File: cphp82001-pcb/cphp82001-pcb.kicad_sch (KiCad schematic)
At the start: 28 parts, among them J1 USB, J2 PAD+, J3 PAD-, Q1 2N7002, Q2 AO3413, U1 BQ21040, U2 TLV75801, U3 MAX40203AUK, U4 APX810-44SA, U5 APX809S-31SA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

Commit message: rev3.5
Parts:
- removed C2: 1n, Capacitor_SMD:C_0805_2012Metric, symbol Device:C
- added C4: 1u, Capacitor_SMD:C_0805_2012Metric, symbol Device:C
- added JP1: NOREG, Resistor_SMD:R_0603_1608Metric, symbol Jumper:SolderJumper_2_Open
- added JP2: NOLIM, Resistor_SMD:R_0603_1608Metric, symbol Jumper:SolderJumper_2_Open
- added R3: 10k, Resistor_SMD:R_0805_2012Metric, symbol Device:R
- added U7: NCP380HSN05, george:SOT-23-5_TI_DBV5, symbol kicad_george:TPS2051B
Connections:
- net EN: now also U3.3 (EN)
- net GND: now also C4.2, R3.1, U7.2 (GND)
- net VOUT: now also C4.1, JP1.2 (B), JP2.1 (A), U7.4 (EN), U7.5 (IN); no longer C7.1, D2.1 (K), J2.1 (Pin_1), U4.3 (VCC)
- net VREG: now also JP1.1 (A)
- new net: R3.2, U7.3 (~{OC})
- new net VOUTF: C7.1, D2.1 (K), J2.1 (Pin_1), JP2.2 (B), U4.3 (VCC), U7.1 (OUT)
- no-connect marks 5 -> 4
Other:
- note added: "3.0~4.2V"
- moved on the sheet: BT1, C3, C5, C7, D2, D3, J2, J3, Q2, R13, R2, R4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

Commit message: Rev 4.0
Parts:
- BT1: value LiPo -> Batt; footprint Connector_JST:JST_SH_BM03B-SRSS-TB_1x03-1MP_P1.00mm_Vertical -> george:JST_SH_BM03B-SRSS-TB_1x03-1MP_P1.00mm_Vertical_13PADS
- D1: value PMEG40T10ERX -> PMEG40T10ERX
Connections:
- net B+: now also JP1.1 (A)
- net VOUT: no longer JP1.2 (B)
- net VREG: now also JP1.2 (B); no longer JP1.1 (A)

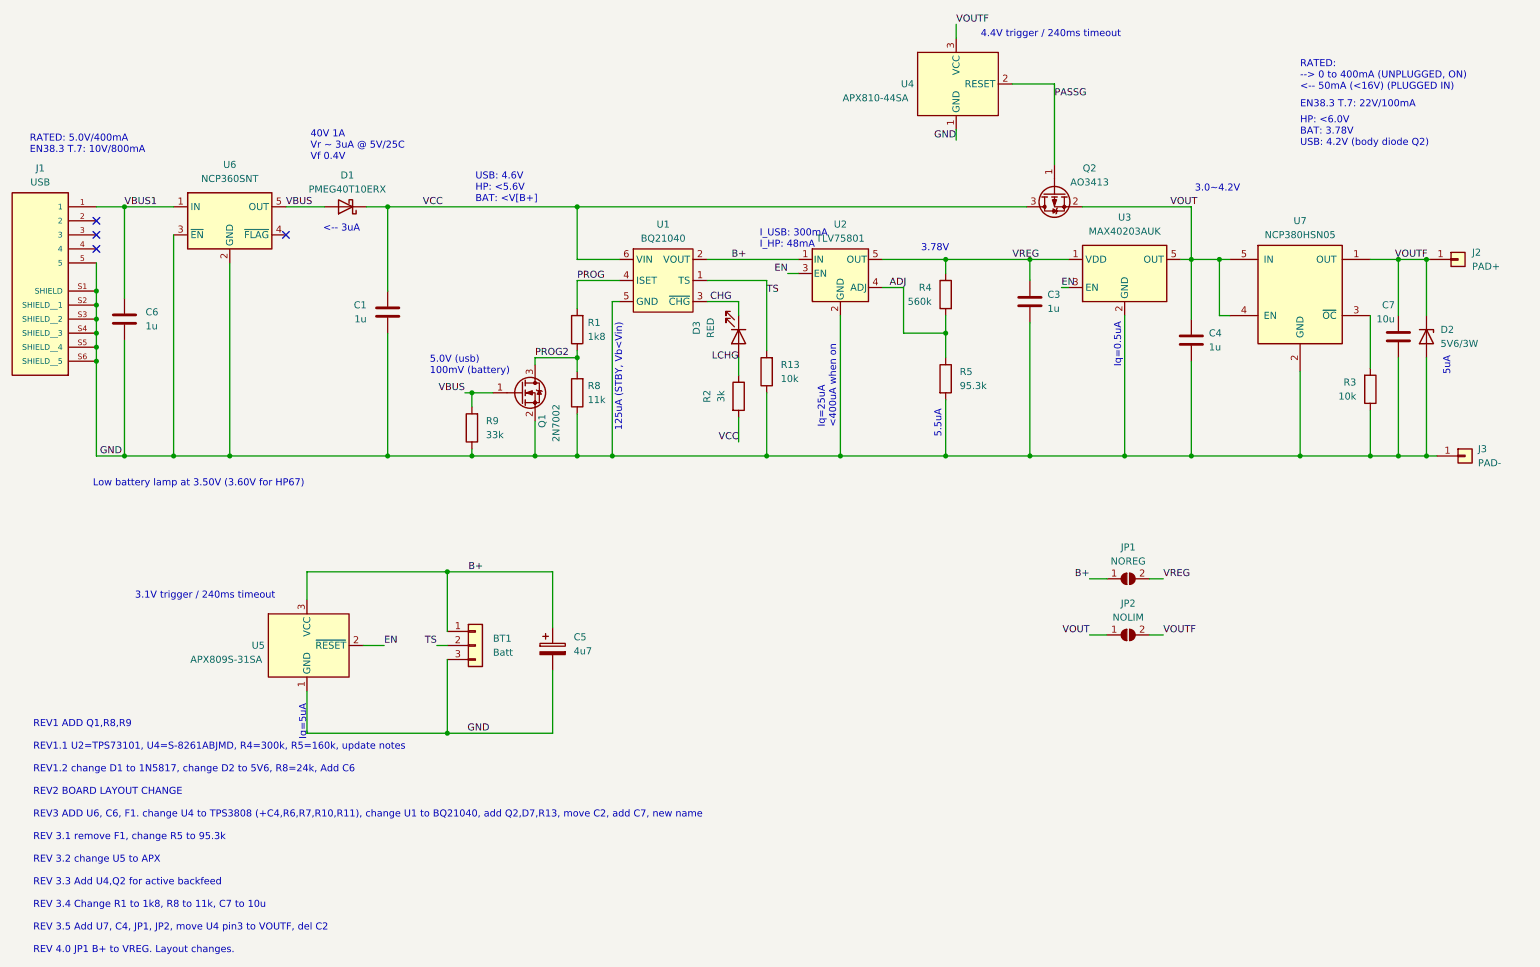
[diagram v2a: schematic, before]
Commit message: Update schematic notes
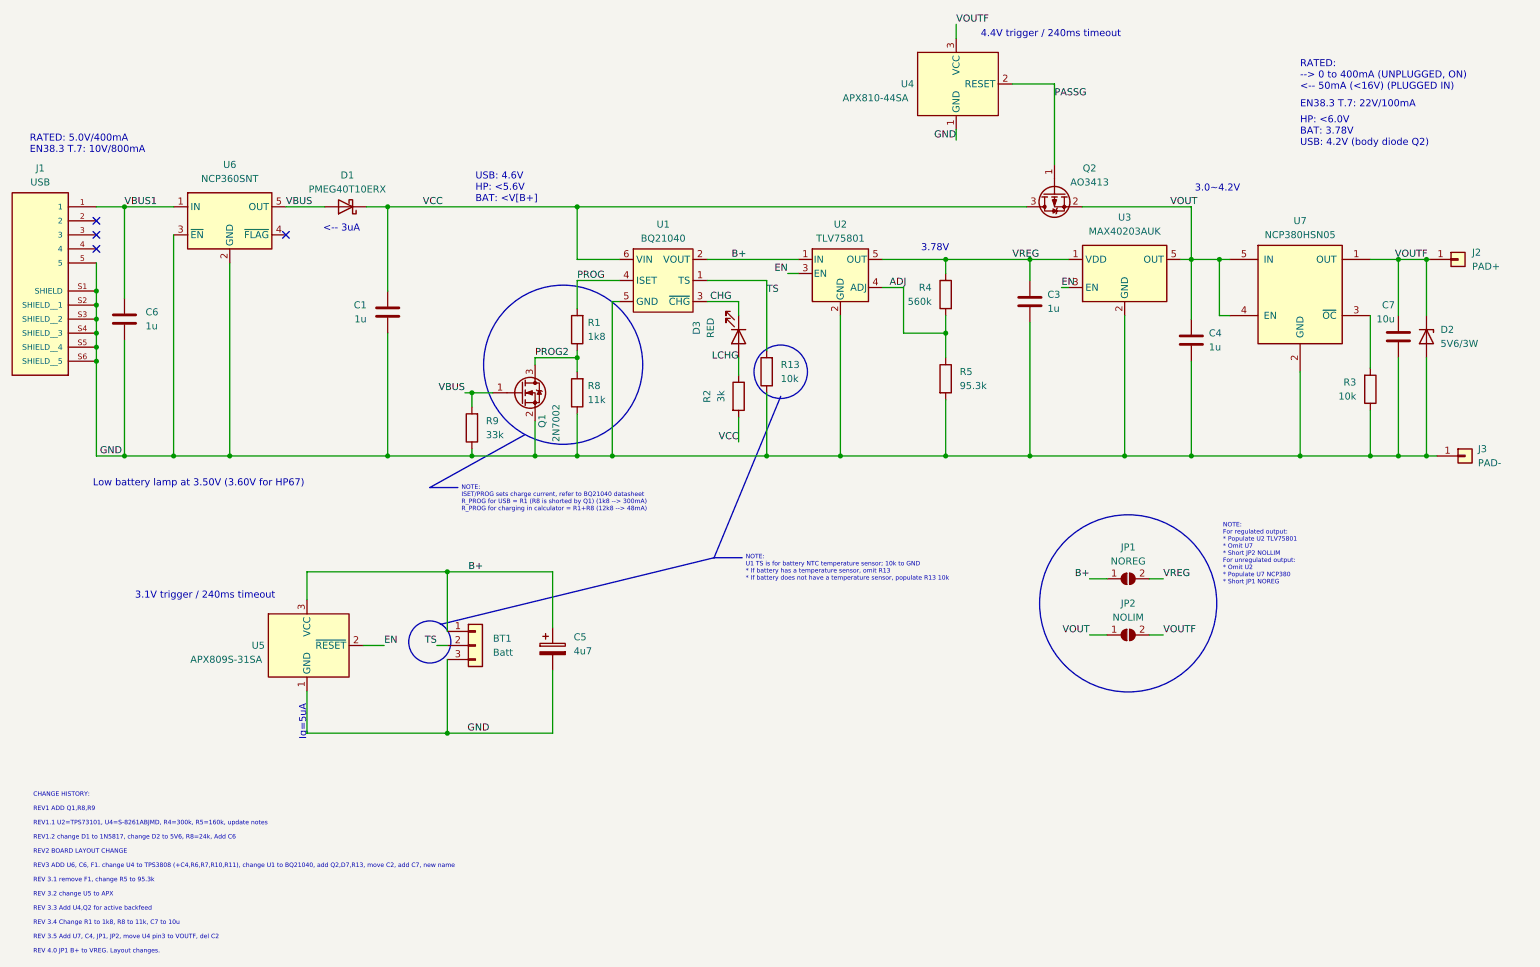
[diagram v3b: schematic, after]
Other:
- note added: "CHANGE HISTORY: REV1 ADD Q1,R8,R9 REV1.1 U2=TPS73101, U4=S-8261ABJMD, R4=300k, R5=160k, update notes REV1.2 change D1 to 1N5817, change D2 to 5V6, R8=24k, Add C6 REV2 BOARD LAYOUT CHANGE REV3 ADD U6, C6, F1. change U4 to TPS3808 (+C4,R6,R7,R10,R11), change U1 to BQ21040, add Q2,D7,R13, move C2, add C7, new name REV 3.1 remove F1, change R5 to 95.3k REV 3.2 change U5 to APX REV 3.3 Add U4,Q2 for a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"
- note added: "NOTE: For regulated output: * Populate U2 TLV75801 * Omit U7 * Short JP2 NOLLIM For unregulated output: * Omit U2 * Populate U7 NCP380 * Short JP1 NOREG"
- note added: "NOTE: ISET/PROG sets charge current, refer to BQ21040 datasheet R_PROG for USB = R1 (R8 is shorted by Q1) (1k8 --> 300mA) R_PROG for charging in calculator = R1+R8 (12k8 --> 48mA)"
- note added: "NOTE: U1 TS is for battery NTC temperature sensor; 10k to GND * If battery has a temperature sensor, omit R13 * If battery does not have a temperature sensor, populate R13 10k"
- note removed: "125uA (STBY, Vb<Vin)"
- note removed: "40V 1A Vr ~ 3uA @ 5V/25C Vf 0.4V"
- note removed: "5.0V (usb) 100mV (battery)"
- note removed: "5.5uA"
- note removed: "5uA"
- note removed: "I_USB: 300mA I_HP: 48mA"
- note removed: "Iq=0.5uA"
- note removed: "Iq=25uA <400uA when on"
- note removed: "REV1 ADD Q1,R8,R9 REV1.1 U2=TPS73101, U4=S-8261ABJMD, R4=300k, R5=160k, update notes REV1.2 change D1 to 1N5817, change D2 to 5V6, R8=24k, Add C6 REV2 BOARD LAYOUT CHANGE REV3 ADD U6, C6, F1. change U4 to TPS3808 (+C4,R6,R7,R10,R11), change U1 to BQ21040, add Q2,D7,R13, move C2, add C7, new name REV 3.1 remove F1, change R5 to 95.3k REV 3.2 change U5 to APX REV 3.3 Add U4,Q2 for active backfeed R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"
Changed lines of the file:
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@@
+		)
+	)
+	(polyline
+		(pts
+			(xy 89.535 109.855) (xy 106.68 100.33)
+		)
+		(stroke
+			(width 0)
+			(type default)
 		)
 	)
@@
 		)
 	)
+	(polyline
+		(pts
+			(xy 140.97 122.555) (xy 153.035 93.345)
+		)
+		(stroke
+			(width 0)
+			(type default)
+		)
+	)
 	(wire
 		(pts
@@
 		)
 	)
+	(polyline
+		(pts
+			(xy 91.44 134.62) (xy 140.97 122.555)
+		)
+		(stroke
+			(width 0)
+			(type default)
+		)
+	)
 	(wire
 		(pts
@@
 		)
 	)
+	(polyline
+		(pts
+			(xy 146.05 122.555) (xy 140.97 122.555)
+		)
+		(stroke
+			(width 0)
+			(type default)
+		)
+	)
 	(wire
 		(pts
@@
 		)
 	)
+	(polyline
+		(pts
+			(xy 94.615 109.855) (xy 89.535 109.855)
+		)
+		(stroke
+			(width 0)
+			(type default)
+		)
+	)
 	(wire
 		(pts
@@
 			(width 0)
 			(type default)
+		)
+	)
+	(circle
+		(center 215.9 130.81)
+		(radius 16.0267)
+		(stroke
+			(width 0)
+			(type default)
+		)
+		(fill
+			(type none)
+		)
+	)
+	(circle
+		(center 89.535 137.795)
+		(radius 3.81)
+		(stroke
+			(width 0)
+			(type default)
+		)
+		(fill
+			(type none)
+		)
+	)
+	(circle
+		(center 153.035 88.9)
+		(radius 4.836)
+		(stroke
+			(width 0)
+			(type default)
+		)
+		(fill
+			(type none)
+		)
+	)
+	(circle
+		(center 113.665 87.63)
+		(radius 14.3964)
+		(stroke
+			(width 0)
+			(type default)
+		)
+		(fill
+			(type none)
 		)
 	)
@@
 		)
 	)
-	(text "I_USB: 300mA\nI_HP: 48mA"
+	(text "NOTE:\nISET/PROG sets charge current, refer to BQ21040 datasheet\nR_PROG for USB = R1 (R8 is shorted by Q1) (1k8 --> 300mA)\nR_PROG for charging in calculator = R1+R8 (12k8 --> 48mA)"
 		(exclude_from_sim no)
-		(at 149.225 66.675 0)
+		(at 95.25 114.3 0)
 		(effects
 			(font
-				(size 1.27 1.27)
+				(size 0.8 0.8)
 			)
 			(justify left bottom)
@@
 		)
 	)
-	(text "Iq=25uA\n<400uA when on"
-		(exclude_from_sim no)
-		(at 163.195 99.06 90)
-		(effects
-			(font
-				(size 1.27 1.27)
-			)
-			(justify left bottom)
-		)
-	)
 	(text "3.1V trigger / 240ms timeout"
 		(exclude_from_sim no)
@@
 		)
 	)
-	(text "5uA"
+	(text "NOTE:\nFor regulated output:\n* Populate U2 TLV75801\n* Omit U7\n* Short JP2 NOLLIM\nFor unregulated output:\n* Omit U2\n* Populate U7 NCP380\n* Short JP1 NOREG\n\n"
 		(exclude_from_sim no)
-		(at 274.32 89.535 90)
+		(at 233.045 122.555 0)
 		(effects
 			(font
-				(size 1.27 1.27)
+				(size 0.8 0.8)
 			)
-			(justify left bottom)
-		)
-	)
-	(text "5.5uA"
+			(justify left)
+		)
+	)
+	(text "NOTE:\nU1 TS is for battery NTC temperature sensor; 10k to GND\n* If battery has a temperature sensor, omit R13\n* If battery does not have a temperature sensor, populate R13 10k\n"
 		(exclude_from_sim no)
-		(at 182.245 100.838 90)
+		(at 146.685 124.46 0)
 		(effects
 			(font
-				(size 1.27 1.27)
+				(size 0.8 0.8)
 			)
-			(justify left bottom)
-		)
-	)
-	(text "125uA (STBY, Vb<Vin)"
-		(exclude_from_sim no)
-		(at 124.46 99.695 90)
-		(effects
-			(font
-				(size 1.27 1.27)
-			)
-			(justify left bottom)
+			(justify left)
 		)
 	)
@@
 		)
 	)
-	(text "5.0V (usb)\n100mV (battery)"
-		(exclude_from_sim no)
-		(at 89.535 89.535 0)
-		(effects
-			(font
-				(size 1.27 1.27)
-			)
-			(justify left bottom)
-		)
-	)
 	(text "RATED: 5.0V/400mA\nEN38.3 T.7: 10V/800mA"
 		(exclude_from_sim no)
@@
 		)
 	)
-	(text "Iq=0.5uA"
-		(exclude_from_sim no)
-		(at 214.757 88.138 90)
-		(effects
-			(font
-				(size 1.27 1.27)
-			)
-			(justify left bottom)
-		)
-	)
-	(text "40V 1A\nVr ~ 3uA @ 5V/25C\nVf 0.4V"
-		(exclude_from_sim no)
-		(at 67.945 50.8 0)
-		(effects
-			(font
-				(size 1.27 1.27)
-			)
-			(justify left bottom)
-		)
-	)
 	(text "Iq=5uA"
 		(exclude_from_sim no)
@@
 		)
 	)
-	(text "REV1 ADD Q1,R8,R9\n\nREV1.1 U2=TPS73101, U4=S-8261ABJMD, R4=300k, R5=160k, update notes\n\nREV1.2 change D1 to 1N5817, change D2 to 5V6, R8=24k, Add C6\n\nREV2 BOARD LAYOUT CHANGE\n\nREV3 ADD U6, C6, F1. change U4 to TPS3808 (+C4,R6,R7,R10,R11), change U1 to BQ21040, add Q2,D7,R13, move C2, add C7, new name\n\nREV 3.1 remove F1, change R5 to 95.3k\n\nREV 3.2 change U5 to APX\n\nREV 3.3 Add U4,Q2 for active backfeed\n\nREV 3.4 Change R1 to 1k8, R8 to 11k, C7 to 10u\n\nREV 3.5 Add U7, C4, JP1, JP2, move U4 pin3 to VOUTF, del C2\n\nREV 4.0 JP1 B+ to VREG. Layout changes."
+	(text "CHANGE HISTORY:\n\nREV1 ADD Q1,R8,R9\n\nREV1.1 U2=TPS73101, U4=S-8261ABJMD, R4=300k, R5=160k, update notes\n\nREV1.2 change D1 to 1N5817, change D2 to 5V6, R8=24k, Add C6\n\nREV2 BOARD LAYOUT CHANGE\n\nREV3 ADD U6, C6, F1. change U4 to TPS3808 (+C4,R6,R7,R10,R11), change U1 to BQ21040, add Q2,D7,R13, move C2, add C7, new name\n\nREV 3.1 remove F1, change R5 to 95.3k\n\nREV 3.2 change U5 to APX\n\nREV 3.3 Add U4,Q2 for active backfeed\n\nREV 3.4 Change R1 to 1k8, R8 to 11k, C7 to 10u\n\nREV 3.5 Add U7, C4, JP1, JP2, move U4 pin3 to VOUTF, del C2\n\nREV 4.0 JP1 B+ to VREG. Layout changes."
 		(exclude_from_sim no)
 		(at 17.78 194.31 0)
 		(effects
 			(font
-				(size 1.27 1.27)
+				(size 0.8 0.8)
 			)
 			(justify left bottom)

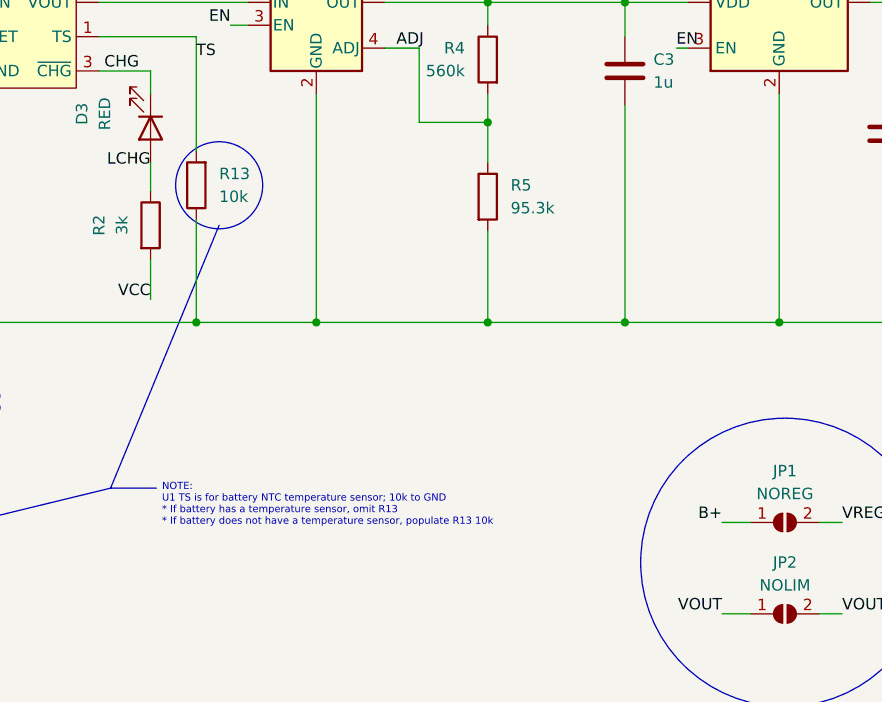
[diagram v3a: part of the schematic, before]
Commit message: Update to charge termination R13 instructions
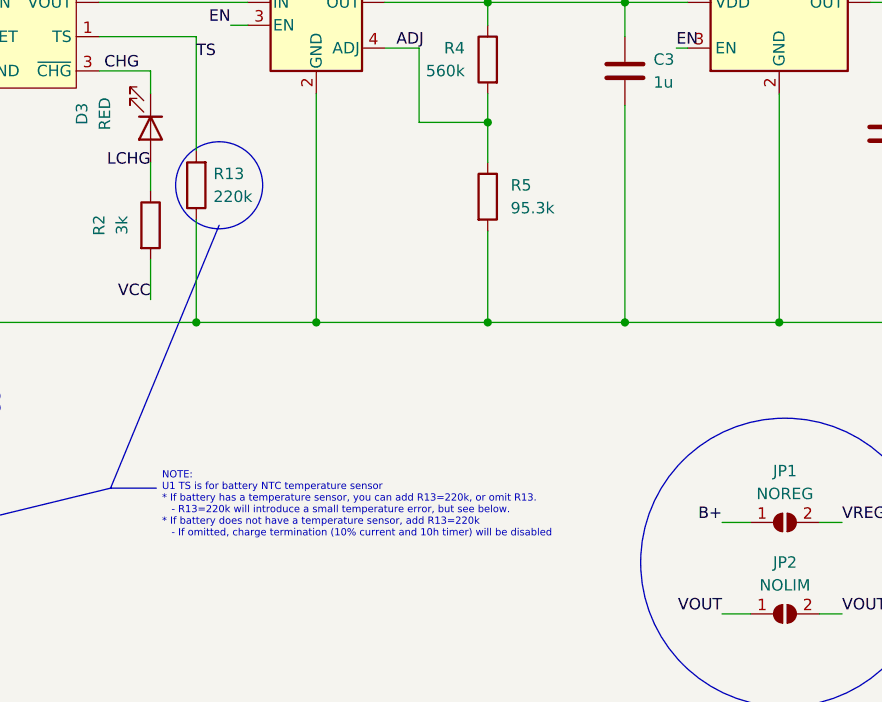
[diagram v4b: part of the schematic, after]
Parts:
- R13: value 10k -> 220k
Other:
- note added: "NOTE: U1 TS is for battery NTC temperature sensor * If battery has a temperature sensor, you can add R13=220k, or omit R13. - R13=220k will introduce a small temperature error, but see below. * If battery does not have a temperature sensor, add R13=220k - If omitted, charge termination (10% current and 10h timer) will be disabled"
- note removed: "NOTE: U1 TS is for battery NTC temperature sensor; 10k to GND * If battery has a temperature sensor, omit R13 * If battery does not have a temperature sensor, populate R13 10k"
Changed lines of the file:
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@@
 		)
 	)
-	(text "NOTE:\nU1 TS is for battery NTC temperature sensor; 10k to GND\n* If battery has a temperature sensor, omit R13\n* If battery does not have a temperature sensor, populate R13 10k\n"
+	(text "NOTE:\nU1 TS is for battery NTC temperature sensor\n* If battery has a temperature sensor, you can add R13=220k, or omit R13.\n   - R13=220k will introduce a small temperature error, but see below.\n* If battery does not have a temperature sensor, add R13=220k\n   - If omitted, charge termination (10% current and 10h timer) will be disabled\n"
 		(exclude_from_sim no)
 		(at 146.685 124.46 0)
@@
 		(fields_autoplaced yes)
 		(property "Reference" "R13"
-			(at 153.035 87.63 0)
+			(at 152.4 87.6299 0)
 			(effects
 				(font
@@
 			)
 		)
-		(property "Value" "10k"
-			(at 153.035 90.17 0)
-			(effects
-				(font
+		(property "Value" "220k"
+			(at 152.4 90.1699 0)
+			(effects
+				(font

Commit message: Amend instructions after testing
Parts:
- R13: value 220k -> 10k
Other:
- note added: "NOTE: U1 TS is for battery NTC temperature sensor * If battery has a temperature sensor, you should omit R13. * If battery does not have a temperature sensor, add R13=10k - If omitted, charge termination (10% current and 10h timer) will be disabled"
- note removed: "NOTE: U1 TS is for battery NTC temperature sensor * If battery has a temperature sensor, you can add R13=220k, or omit R13. - R13=220k will introduce a small temperature error, but see below. * If battery does not have a temperature sensor, add R13=220k - If omitted, charge termination (10% current and 10h timer) will be disabled"
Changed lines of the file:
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@@
 		)
 	)
-	(text "NOTE:\nU1 TS is for battery NTC temperature sensor\n* If battery has a temperature sensor, you can add R13=220k, or omit R13.\n   - R13=220k will introduce a small temperature error, but see below.\n* If battery does not have a temperature sensor, add R13=220k\n   - If omitted, charge termination (10% current and 10h timer) will be disabled\n"
+	(text "NOTE:\nU1 TS is for battery NTC temperature sensor\n* If battery has a temperature sensor, you should omit R13.\n* If battery does not have a temperature sensor, add R13=10k\n   - If omitted, charge termination (10% current and 10h timer) will be disabled\n"
 		(exclude_from_sim no)
 		(at 146.685 124.46 0)
@@
 			)
 		)
-		(property "Value" "220k"
+		(property "Value" "10k"
 			(at 152.4 90.1699 0)
 			(effects

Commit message: rev5
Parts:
- removed C3: 1u, Capacitor_SMD:C_0805_2012Metric, symbol Device:C
- removed JP1: NOREG, Resistor_SMD:R_0603_1608Metric, symbol Jumper:SolderJumper_2_Open
- removed JP2: NOLIM, Resistor_SMD:R_0603_1608Metric, symbol Jumper:SolderJumper_2_Open
- removed R3: 10k, Resistor_SMD:R_0805_2012Metric, symbol Device:R
- removed R4: 560k, Resistor_SMD:R_0805_2012Metric, symbol Device:R
- removed R5: 95.3k, Resistor_SMD:R_0805_2012Metric, symbol Device:R
- removed U2: TLV75801, george:SOT-23-5_TI_DBV5, symbol Regulator_Linear:MIC5205YM5
- added D4: 1N4148W, Diode_SMD:D_SOD-123, symbol Diode:1N4148W
- R8: value 11k -> 9k1
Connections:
- net VREG is gone; now on net B+: U3.1 (VDD)
- net CHG: now also R2.1; no longer D3.1 (K)
- net LCHG: now also D3.1 (K), R2.2; no longer D3.2 (A), R2.1
- net VCC: now also D3.2 (A), D4.1 (K); no longer Q2.3 (D), R2.2
- new net: D4.2 (A), Q2.3 (D)
- no-connect marks 4 -> 5
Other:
- note added: "0.8V drop @ 50mA"
- note added: "3.1V trigger 240ms timeout"
- note added: "3.1~4.3V"
- note added: "4.4V trigger 240ms timeout"
- note added: "HP: <6.0V BAT: 3.1~4.3V USB: NONE"
- note added: "NOTE: ISET/PROG sets charge current, refer to BQ21040 datasheet R_PROG for USB = R1 (R8 is shorted by Q1) (1k3 --> 415mA). Adjust for 0.2C (1k8 for 1500mAh, 1k3 for 2000mAh). R_PROG for charging in calculator = R1+R8 (10.4k --> 50.7mA) - note BQ21040 will limit current as supplied below VCC=4.3V."
- note added: "USB: 4.6V HP: 3.6~5.6V BAT: <V[B+]"
- note removed: "3.0~4.2V"
- note removed: "3.1V trigger / 240ms timeout"
- note removed: "3.78V"
- note removed: "4.4V trigger / 240ms timeout"
- note removed: "HP: <6.0V BAT: 3.78V USB: 4.2V (body diode Q2)"
- note removed: "Iq=5uA"
- note removed: "NOTE: For regulated output: * Populate U2 TLV75801 * Omit U7 * Short JP2 NOLLIM For unregulated output: * Omit U2 * Populate U7 NCP380 * Short JP1 NOREG"
- note removed: "NOTE: ISET/PROG sets charge current, refer to BQ21040 datasheet R_PROG for USB = R1 (R8 is shorted by Q1) (1k8 --> 300mA) R_PROG for charging in calculator = R1+R8 (12k8 --> 48mA)"
- note removed: "USB: 4.6V HP: <5.6V BAT: <V[B+]"
- moved on the sheet: BT1, C5, D3, Q1, R1, R13, R2, R8, R9, U1, U5
